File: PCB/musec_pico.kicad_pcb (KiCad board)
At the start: 2 copper layers, 218 x 128.1 mm, 44 parts, among them SW1 SW_DIP_x01, SW2 SW_DIP_x01, SW3 SW_DIP_x01, SW4 SW_DIP_x01, SW5 SW_DIP_x01, SW6 SW_DIP_x01, SW7 SW_DIP_x01, U1 PiPico, U3 TMAG5273, U4 TMAG5273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

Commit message: PCB progress 70%
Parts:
- added JA1: Conn_01x04, musec_pico:SH1.0_4P_Solder_Combo, B.Cu at (151.2, 145.1)
- added JA2: Conn_01x04, musec_pico:SH1.0_4P_Solder_Combo, B.Cu at (189.2, 145.1)
- added JA3: Conn_01x04, musec_pico:SH1.0_4P_Solder_Combo, B.Cu at (227.2, 145.1)
- added JA4: Conn_01x04, musec_pico:SH1.0_4P_Solder_Combo, B.Cu at (265.2, 145.1)
- added JA5: Conn_01x04, musec_pico:SH1.0_4P_Solder_Combo, B.Cu at (303.2, 145.1)
- added JB1: Conn_01x04, musec_pico:SH1.0_4P_Solder_Combo, B.Cu at (138.2, 159.1)
- added JB2: Conn_01x04, musec_pico:SH1.0_4P_Solder_Combo, B.Cu at (176.2, 159.1)
- added JB3: Conn_01x04, musec_pico:SH1.0_4P_Solder_Combo, B.Cu at (214.2, 159.1)
- added JB4: Conn_01x04, musec_pico:SH1.0_4P_Solder_Combo, B.Cu at (252.2, 159.1)
- added JB5: Conn_01x04, musec_pico:SH1.0_4P_Solder_Combo, B.Cu at (290.2, 159.1)
- R1, R2, USB1: moved to F.Cu
- U3, U4, U7, U8, U9: footprint Package_TO_SOT_SMD:TSOT-23-6_HandSoldering -> Package_TO_SOT_SMD:SOT-23-6
- moved R3 27.1 mm to (143.6, 121.7)
- moved D19 16.0 mm to (303.2, 104.1)
- moved D20 16.0 mm to (303.2, 120.1)
- moved R1 6.08 mm to (217.2, 79.1), turned to 0 degrees
- moved R2 6.08 mm to (211.2, 79.1), turned to 180 degrees
- turned USB1 to 180 degrees
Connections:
- C1 pad 1: +3V3 -> /VB1
- C2 pad 1: +3V3 -> /VB2
- C3 pad 1: +3V3 -> /VB3
- C4 pad 1: +3V3 -> /VB4
- C5 pad 1: +3V3 -> /VB5
- U1 pad 1: /SDA0 -> /SDA
- U1 pad 11: /AUDIO_L -> unconnected-(U1-GPIO8-Pad11)
- U1 pad 12: unconnected-(U1-GPIO9-Pad12) -> /VB5
- U1 pad 14: unconnected-(U1-GPIO10-Pad14) -> /VB4
- U1 pad 15: unconnected-(U1-GPIO11-Pad15) -> /VB3
- U1 pad 16: unconnected-(U1-GPIO12-Pad16) -> /VB2
- U1 pad 17: unconnected-(U1-GPIO13-Pad17) -> /VB1
- U1 pad 2: /SCL0 -> /SCL
- U1 pad 9: /AUDIO_R -> unconnected-(U1-GPIO6-Pad9)
- U3 pad 1: Net-(U3-SCL) -> /SCL
- U3 pad 2: Net-(U3-GND) -> GND
- U3 pad 3: Net-(U3-GND) -> GND
- U3 pad 6: Net-(U3-SDA) -> /SDA
- U4 pad 1: Net-(U3-SCL) -> /SCL
- U4 pad 2: Net-(U3-GND) -> GND
- U4 pad 3: Net-(U3-GND) -> GND
- U4 pad 6: Net-(U3-SDA) -> /SDA
- U7 pad 1: Net-(U3-SCL) -> /SCL
- U7 pad 2: Net-(U3-GND) -> GND
- U7 pad 3: Net-(U3-GND) -> GND
- U7 pad 6: Net-(U3-SDA) -> /SDA
- U8 pad 1: Net-(U3-SCL) -> /SCL
- U8 pad 2: Net-(U3-GND) -> GND
- U8 pad 3: Net-(U3-GND) -> GND
- U8 pad 6: Net-(U3-SCL) -> /SCL
- U9 pad 1: Net-(U3-SCL) -> /SCL
- U9 pad 2: Net-(U3-GND) -> GND
- U9 pad 3: Net-(U3-GND) -> GND
- U9 pad 6: Net-(U3-SDA) -> /SDA
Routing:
- net +5V: track 0.00 -> 797.1 mm, vias 0 -> 5
- net /SDA: track 0.00 -> 408.0 mm, vias 0 -> 5
- net /SCL: track 0.00 -> 344.2 mm, vias 0 -> 7
- net GND: track 0.00 -> 307.0 mm, vias 0 -> 5
- net /VB1: track 0.00 -> 265.2 mm, vias 0 -> 7
- net /K4: track 0.00 -> 156.8 mm
- net /K5: track 0.00 -> 138.9 mm
- net Net-(D21-Out): track 0.00 -> 127.3 mm, vias 0 -> 2
- net /K7: track 0.00 -> 120.4 mm
- net /VB2: track 0.00 -> 69.0 mm, vias 0 -> 4
- net /K3: track 0.00 -> 68.2 mm
- net Net-(D20-Out): track 0.00 -> 67.3 mm
- net Net-(D16-Out): track 0.00 -> 52.5 mm, vias 0 -> 2
- net Net-(D8-Out): track 0.00 -> 52.5 mm
- net Net-(D4-Out): track 0.00 -> 51.0 mm
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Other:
- outline, holes or cut-outs redrawn

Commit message: PCB almost done (95%)
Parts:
- removed U8, U9: TMAG5273, Package_TO_SOT_SMD:SOT-23-6
- added U5: TMAG5273, Package_TO_SOT_SMD:SOT-23-6, F.Cu at (214.2, 141.6)
- added U6: TMAG5273, Package_TO_SOT_SMD:SOT-23-6, F.Cu at (252.2, 141.6)
- moved U7 76.0 mm to (290.2, 141.6)
- moved R3 6.40 mm to (146.5, 116.0)
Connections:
- D17 pad G: Net-(D17-VSS) -> GND
- D18 pad G: Net-(D17-VSS) -> GND
- D19 pad G: Net-(D17-VSS) -> GND
- D20 pad G: Net-(D17-VSS) -> GND
- D21 pad G: Net-(D17-VSS) -> GND
- D22 pad G: Net-(D17-VSS) -> GND
- U4 pad 4: /VB3 -> /VB2
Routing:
- net /SDA: track 408.0 -> 606.1 mm, vias 5 -> 14
- net /SCL: track 344.2 -> 532.6 mm, vias 7 -> 17
- net /VB5: track 29.4 -> 212.8 mm, vias 2 -> 5
- net /VB1: track 265.2 -> 99.4 mm, vias 7 -> 3
- net /VB4: track 29.4 -> 180.1 mm, vias 2 -> 5
- net /VB3: track 29.4 -> 143.0 mm, vias 2 -> 5
- net /K2: track 0.00 -> 96.3 mm, vias 0 -> 1
- net GND: track 307.0 -> 358.3 mm, vias 5 -> 65
- net /VB2: track 69.0 -> 116.3 mm, vias 4 -> 5
- net +5V: track 797.1 -> 764.7 mm, vias 5 -> 9
- net Net-(D1-In): track 0.00 -> 21.9 mm, vias 0 -> 1
- net /K4: track 156.8 -> 166.7 mm, vias 0 -> 1
- net Net-(U1-GPIO14): track 0.00 -> 8.68 mm
- added copper zone on B.Cu, net GND
- added copper zone on F.Cu, net GND
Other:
- board text added: "Musec Pico"
- board text added: "v1.0"

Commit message: PCB v1.0
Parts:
- added C10: 0.1uF, Capacitor_SMD:C_0603_1608Metric_Pad1.08x0.95mm_HandSolder, F.Cu at (274.6, 112.5)
- added C6: 0.1uF, Capacitor_SMD:C_0603_1608Metric_Pad1.08x0.95mm_HandSolder, F.Cu at (123.0, 110.5)
- added C7: 0.1uF, Capacitor_SMD:C_0603_1608Metric_Pad1.08x0.95mm_HandSolder, F.Cu at (159.1, 184.6)
- added C8: 0.1uF, Capacitor_SMD:C_0603_1608Metric_Pad1.08x0.95mm_HandSolder, F.Cu at (198.6, 112.4)
- added C9: 0.1uF, Capacitor_SMD:C_0603_1608Metric_Pad1.08x0.95mm_HandSolder, F.Cu at (235.1, 187.7)
- turned SW2 to 180 degrees
- turned SW4 to 180 degrees
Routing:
- net /K4: track 166.7 -> 183.1 mm
- net /K2: track 96.3 -> 112.4 mm
- net /SDA: track 606.1 -> 609.9 mm
- net +5V: track 764.7 -> 768.1 mm
- net GND: track 358.3 -> 355.8 mm, vias 65 -> 69
- net /VB5: track 212.8 -> 212.1 mm
- net /VB4: track 180.1 -> 179.4 mm
- net /VB3: track 143.0 -> 142.3 mm
- net /VB2: track 116.3 -> 115.6 mm
- net /VB1: track 99.4 -> 98.7 mm
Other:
- outline, holes or cut-outs redrawn

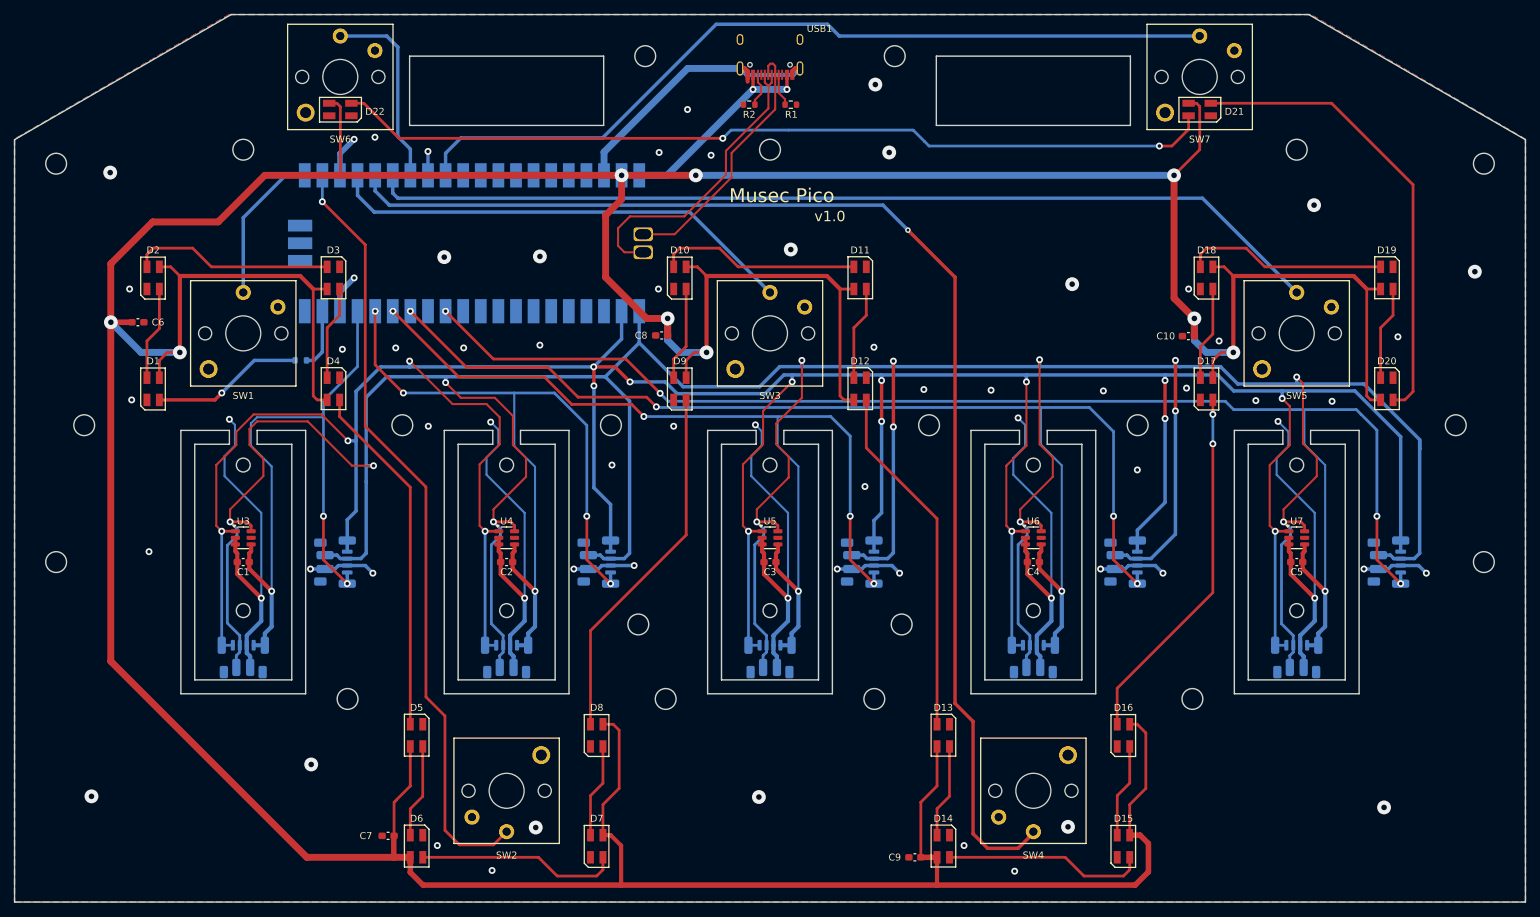
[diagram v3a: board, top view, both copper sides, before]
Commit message: PCB v1.1 to support pedal
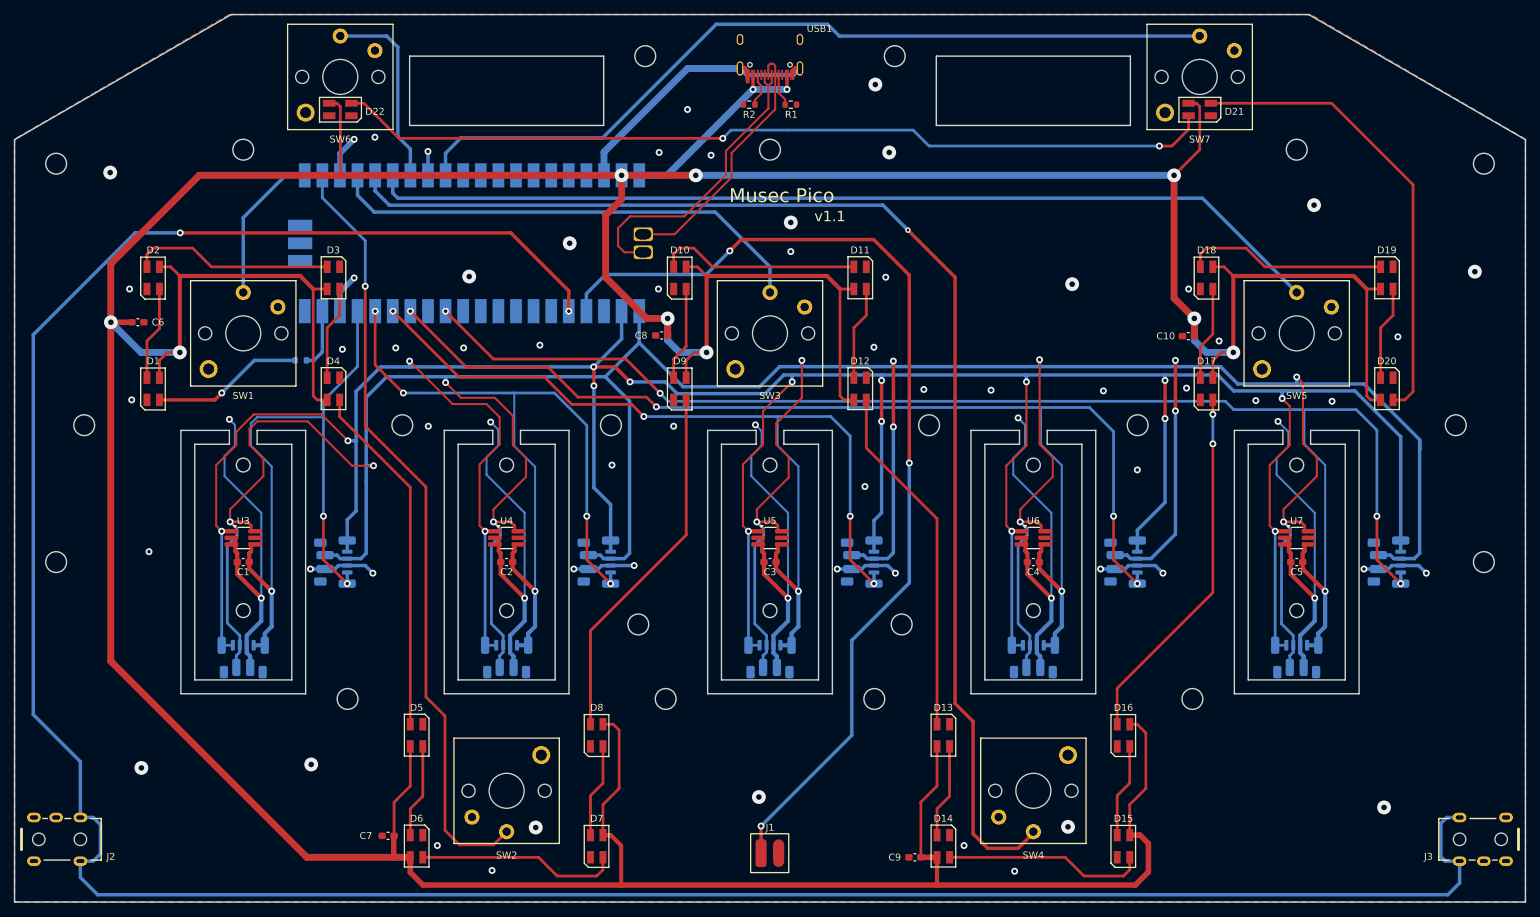
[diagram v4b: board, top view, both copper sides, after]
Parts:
- added J1: Conn_01x02, musec_pico:Solder_2P, F.Cu at (214.2, 187.1)
- added J2: PJ313, musec_pico:PJ313, F.Cu at (114.7, 185.1)
- added J3: PJ313, musec_pico:PJ313, F.Cu at (313.7, 185.1)
- U3, U4, U5, U6, U7: footprint Package_TO_SOT_SMD:SOT-23-6 -> Package_TO_SOT_SMD:TSOT-23-6_HandSoldering
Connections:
- U1 pad 4: unconnected-(U1-GPIO2-Pad4) -> Net-(J1-Pin_1)
- U1 pad 5: unconnected-(U1-GPIO3-Pad5) -> Net-(J2-T)
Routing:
- net Net-(J2-T): track 0.00 -> 390.2 mm, vias 0 -> 2
- net Net-(J1-Pin_1): track 0.00 -> 146.7 mm, vias 0 -> 3
- net /K3: track 68.2 -> 70.4 mm
- net GND: track 355.8 -> 355.2 mm, vias 69 -> 71
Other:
- board text added: "v1.1"
- board text removed: "v1.0"

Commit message: PCB v1.2 (internal pedal connector and light)
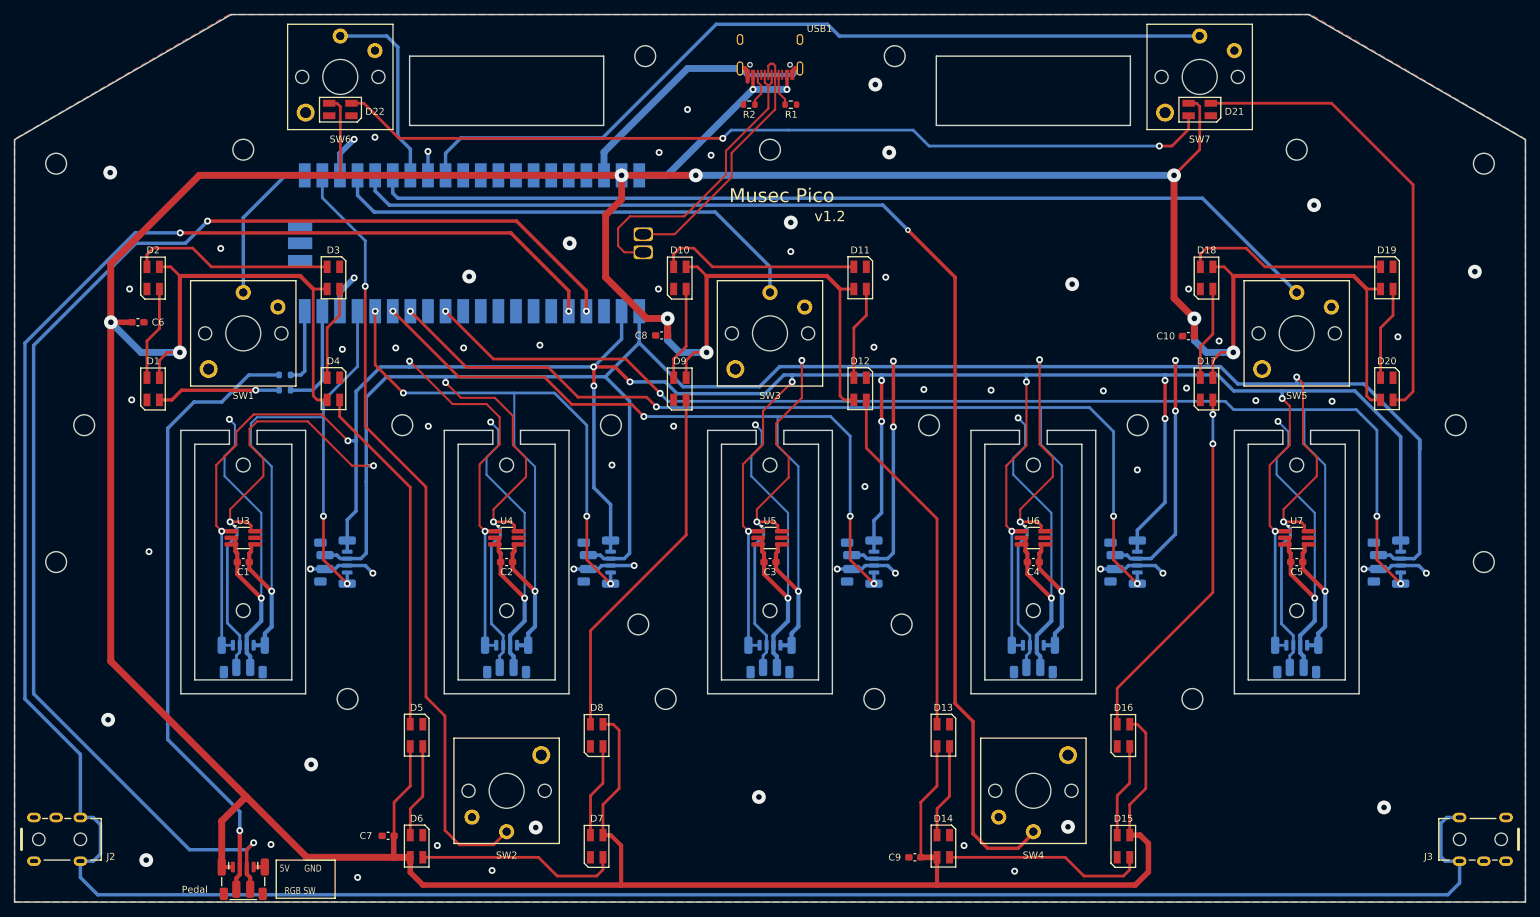
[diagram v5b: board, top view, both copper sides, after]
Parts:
- added R4: 10, Resistor_SMD:R_0603_1608Metric, B.Cu at (144.2, 118.1)
- J1: value Conn_01x02 -> Pedal; footprint musec_pico:Solder_2P -> musec_pico:SH1.0_4P_Solder_Combo
- moved J1 76.1 mm to (138.2, 191.1), turned to 0 degrees
- moved R3 4.88 mm to (144.2, 120.3)
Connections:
- J1 pad 1: Net-(J1-Pin_1) -> +5V
- J1 pad 2: GND -> Net-(J1-Pin_2)
- U1 pad 20: unconnected-(U1-GPIO15-Pad20) -> Net-(U1-GPIO15)
- U1 pad 4: Net-(J1-Pin_1) -> Net-(J1-Pin_3)
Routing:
- net Net-(J1-Pin_3): track 0.00 -> 193.3 mm, vias 0 -> 3
- net Net-(J1-Pin_1): track 146.7 -> 0.00 mm, vias 3 -> 0
- net Net-(J1-Pin_2): track 0.00 -> 90.3 mm, vias 0 -> 1
- net +5V: track 768.1 -> 781.3 mm
- net Net-(U1-GPIO15): track 0.00 -> 10.9 mm
- net Net-(U1-GPIO14): track 8.68 -> 15.2 mm
- net Net-(D1-In): track 21.9 -> 17.9 mm
- net GND: track 355.2 -> 356.8 mm, vias 71 -> 75
- net Net-(J2-T): track 390.2 -> 391.1 mm
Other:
- board text added: "5V GND RGB SW"
- board text added: "v1.2"
- board text removed: "v1.1"

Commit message: PCB V1.21, larger thru-holes for PJ313
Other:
- board text added: "v1.21"
- board text removed: "v1.2"
